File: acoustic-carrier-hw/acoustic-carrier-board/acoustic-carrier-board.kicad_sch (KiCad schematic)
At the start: 0 parts

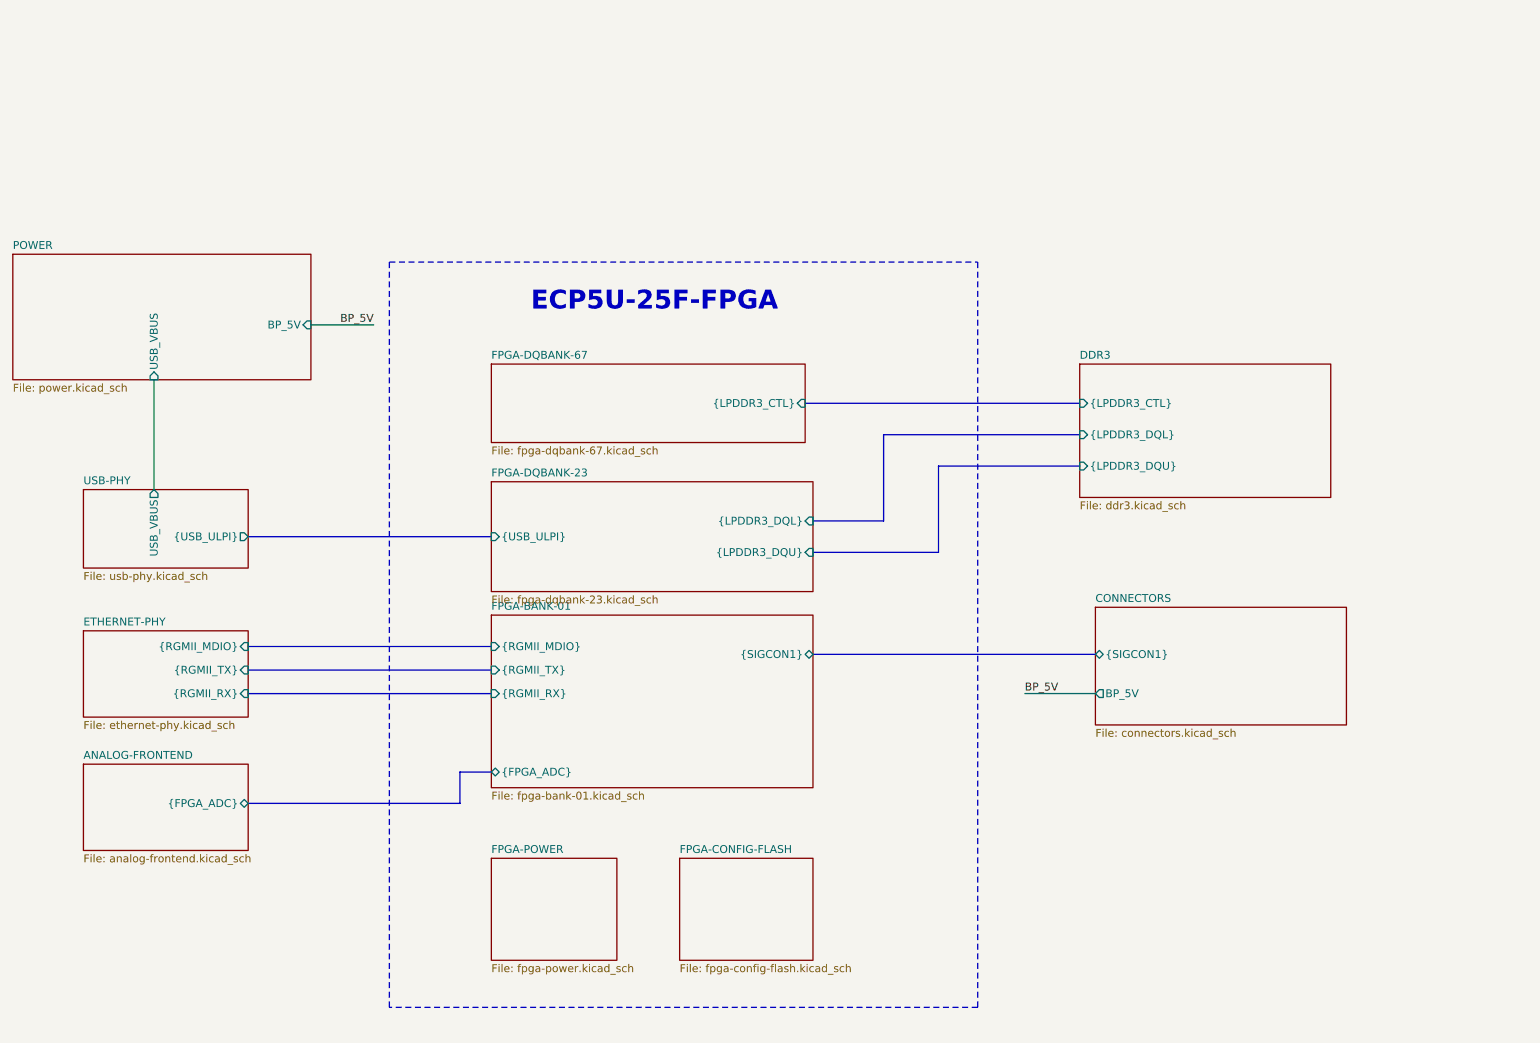
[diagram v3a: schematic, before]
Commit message: [carrier] Added decoupling caps to flash and comparators
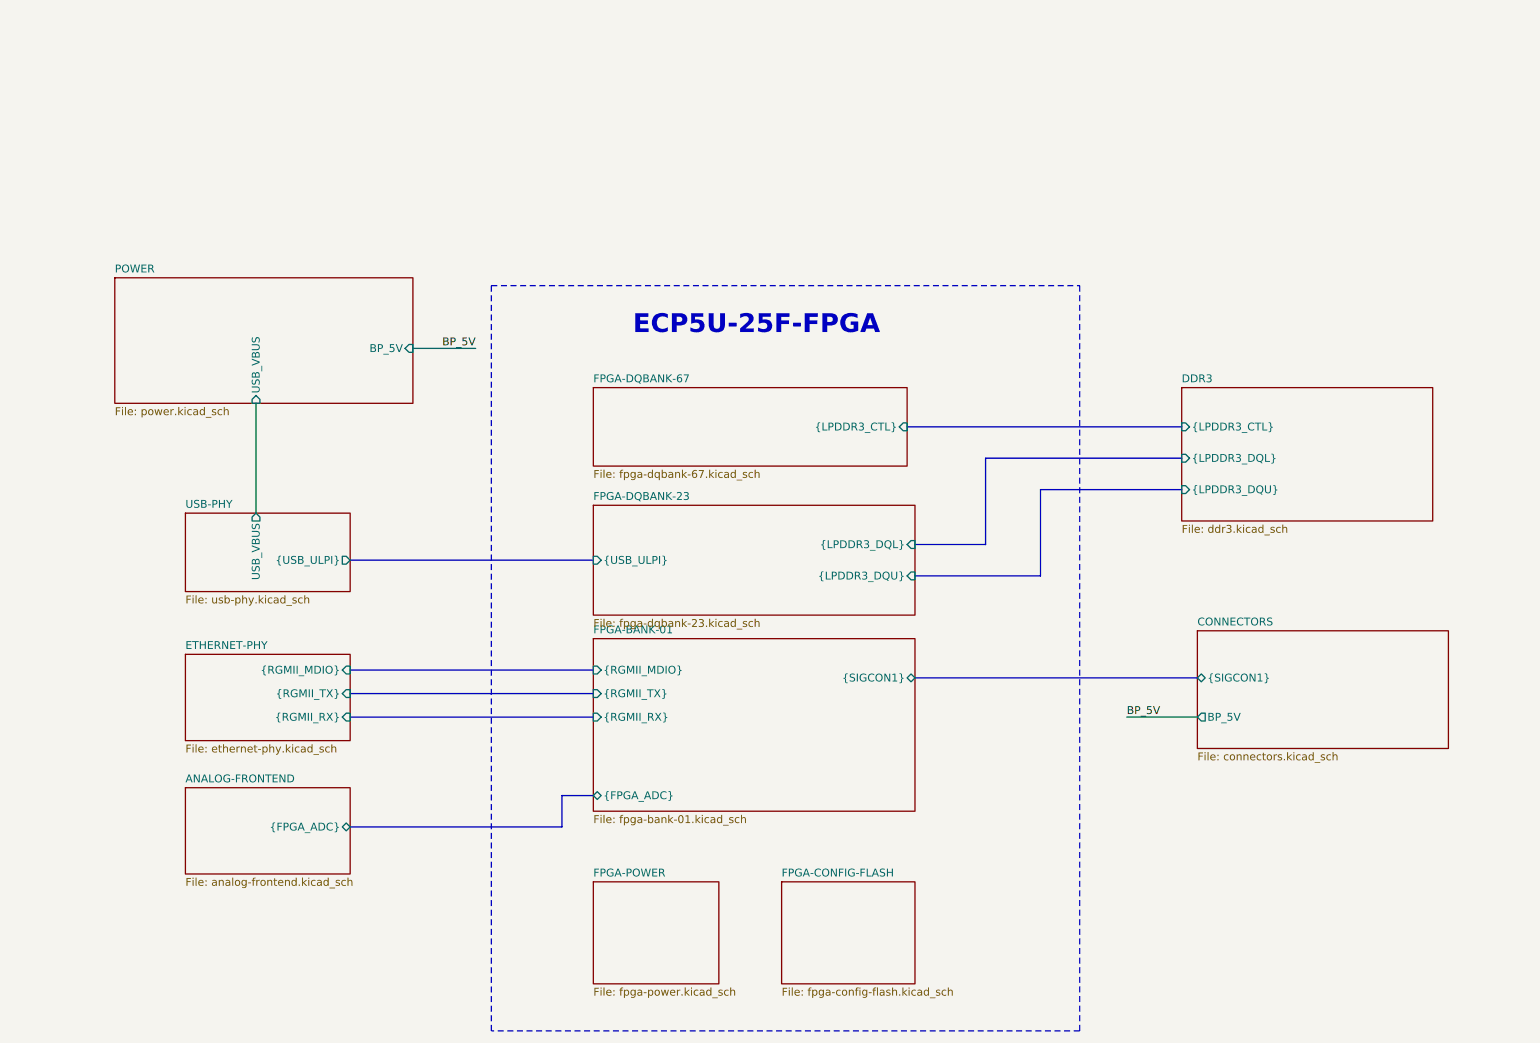
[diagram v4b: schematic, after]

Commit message: [carrier] Added extra decoupling to ECP5U according to datasheet (next) perform page-wise checks, add testpoints
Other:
- sheet CONNECTORS ports: added none; removed BP_5V
- sheet POWER ports: added none; removed BP_5V
- note added: "CONNECTORS - Connectors bound to a peripheral are kept in the same schematic - Connectors indifferent to FPGA bank are put in "connectors""
- note added: "DESIGN RULES"
- note added: "GENERAL FPGA NOTES"
- note added: "POWER RECOMMENDATIONS - Check 3.1 TN-02038 for filtering and decoupling - Used banks: extra decoupling capacitance"
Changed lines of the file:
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@@
+		)
+	)
+	(text "GENERAL FPGA NOTES"
+		(exclude_from_sim no)
+		(at 103.886 -9.652 0)
+		(effects
+			(font
+				(size 2.54 2.54)
+			)
+			(justify left bottom)
 		)
 	)
@@
 		)
 	)
-	(bus
-		(pts
-			(xy 180.34 57.15) (xy 212.09 57.15)
-		)
-		(stroke
-			(width 0)
-			(type default)
-		)
-	)
-	(bus
-		(pts
-			(xy 116.84 111.76) (xy 111.76 111.76)
-		)
-		(stroke
-			(width 0)
-			(type default)
-		)
-	)
-	(bus
-		(pts
-			(xy 189.23 62.23) (xy 212.09 62.23)
-		)
-		(stroke
-			(width 0)
-			(type default)
-		)
-	)
-	(bus
-		(pts
-			(xy 111.76 116.84) (xy 77.47 116.84)
-		)
-		(stroke
-			(width 0)
-			(type default)
-		)
-	)
-	(wire
-		(pts
-			(xy 62.23 48.26) (xy 62.23 66.04)
-		)
-		(stroke
-			(width 0)
-			(type default)
-		)
-	)
-	(wire
-		(pts
-			(xy 87.63 39.37) (xy 97.79 39.37)
-		)
-		(stroke
-			(width 0)
-			(type default)
-		)
-	)
-	(bus
-		(pts
-			(xy 77.47 73.66) (xy 116.84 73.66)
-		)
-		(stroke
-			(width 0)
-			(type default)
-		)
-	)
-	(bus
-		(pts
-			(xy 167.64 52.07) (xy 212.09 52.07)
-		)
-		(stroke
-			(width 0)
-			(type default)
-		)
-	)
-	(bus
-		(pts
-			(xy 189.23 76.2) (xy 168.91 76.2)
-		)
-		(stroke
-			(width 0)
-			(type default)
-		)
-	)
-	(bus
-		(pts
-			(xy 180.34 57.15) (xy 180.34 71.12)
-		)
-		(stroke
-			(width 0)
-			(type default)
-		)
-	)
-	(bus
-		(pts
-			(xy 111.76 111.76) (xy 111.76 116.84)
-		)
-		(stroke
-			(width 0)
-			(type default)
-		)
-	)
-	(bus
-		(pts
-			(xy 77.47 91.44) (xy 116.84 91.44)
-		)
-		(stroke
-			(width 0)
-			(type default)
-		)
-	)
-	(bus
-		(pts
-			(xy 168.91 92.71) (xy 214.63 92.71)
-		)
-		(stroke
-			(width 0)
-			(type default)
-		)
-	)
-	(bus
-		(pts
-			(xy 189.23 62.23) (xy 189.23 76.2)
-		)
-		(stroke
-			(width 0)
-			(type default)
-		)
-	)
-	(bus
-		(pts
-			(xy 77.47 99.06) (xy 116.84 99.06)
-		)
-		(stroke
-			(width 0)
-			(type default)
-		)
-	)
-	(wire
-		(pts
-			(xy 203.2 99.06) (xy 214.63 99.06)
-		)
-		(stroke
-			(width 0)
-			(type default)
-		)
-	)
-	(bus
-		(pts
-			(xy 77.47 95.25) (xy 116.84 95.25)
-		)
-		(stroke
-			(width 0)
-			(type default)
-		)
-	)
-	(bus
-		(pts
-			(xy 180.34 71.12) (xy 168.91 71.12)
-		)
-		(stroke
-			(width 0)
-			(type default)
-		)
-	)
-	(label "BP_5V"
-		(at 203.2 99.06 0)
+	(text "POWER RECOMMENDATIONS\n- Check 3.1 TN-02038 for filtering and decoupling\n- Used banks: extra decoupling capacitance"
+		(exclude_from_sim no)
+		(at 104.394 -1.778 0)
 		(effects
 			(font
@@
 		)
 	)
-	(label "BP_5V"
-		(at 97.79 39.37 180)
+	(text "CONNECTORS\n- Connectors bound to a peripheral are kept in the same schematic\n- Connectors indifferent to FPGA bank are put in \"connectors\""
+		(exclude_from_sim no)
+		(at 188.468 -2.794 0)
 		(effects
 			(font
 				(size 1.27 1.27)
 			)
-			(justify right bottom)
+			(justify left bottom)
+		)
+	)
+	(text "DESIGN RULES"
+		(exclude_from_sim no)
+		(at 187.96 -10.668 0)
+		(effects
+			(font
+				(size 2.54 2.54)
+			)
+			(justify left bottom)
+		)
+	)
+	(bus
+		(pts
+			(xy 180.34 57.15) (xy 212.09 57.15)
+		)
+		(stroke
+			(width 0)
+			(type default)
+		)
+	)
+	(bus
+		(pts
+			(xy 116.84 111.76) (xy 111.76 111.76)
+		)
+		(stroke
+			(width 0)
+			(type default)
+		)
+	)
+	(bus
+		(pts
+			(xy 189.23 62.23) (xy 212.09 62.23)
+		)
+		(stroke
+			(width 0)
+			(type default)
+		)
+	)
+	(bus
+		(pts
+			(xy 111.76 116.84) (xy 77.47 116.84)
+		)
+		(stroke
+			(width 0)
+			(type default)
+		)
+	)
+	(wire
+		(pts
+			(xy 62.23 48.26) (xy 62.23 66.04)
+		)
+		(stroke
+			(width 0)
+			(type default)
+		)
+	)
+	(bus
+		(pts
+			(xy 77.47 73.66) (xy 116.84 73.66)
+		)
+		(stroke
+			(width 0)
+			(type default)
+		)
+	)
+	(bus
+		(pts
+			(xy 167.64 52.07) (xy 212.09 52.07)
+		)
+		(stroke
+			(width 0)
+			(type default)
+		)
+	)
+	(bus
+		(pts
+			(xy 189.23 76.2) (xy 168.91 76.2)
+		)
+		(stroke
+			(width 0)
+			(type default)
+		)
+	)
+	(bus
+		(pts
+			(xy 180.34 57.15) (xy 180.34 71.12)
+		)
+		(stroke
+			(width 0)
+			(type default)
+		)
+	)
+	(bus
+		(pts
+			(xy 111.76 111.76) (xy 111.76 116.84)
+		)
+		(stroke
+			(width 0)
+			(type default)
+		)
+	)
+	(bus
+		(pts
+			(xy 77.47 91.44) (xy 116.84 91.44)
+		)
+		(stroke
+			(width 0)
+			(type default)
+		)
+	)
+	(bus
+		(pts
+			(xy 168.91 92.71) (xy 213.36 92.71)
+		)
+		(stroke
+			(width 0)
+			(type default)
+		)
+	)
+	(bus
+		(pts
+			(xy 189.23 62.23) (xy 189.23 76.2)
+		)
+		(stroke
+			(width 0)
+			(type default)
+		)
+	)
+	(bus
+		(pts
+			(xy 77.47 99.06) (xy 116.84 99.06)
+		)
+		(stroke
+			(width 0)
+			(type default)
+		)
+	)
+	(bus
+		(pts
+			(xy 77.47 95.25) (xy 116.84 95.25)
+		)
+		(stroke
+			(width 0)
+			(type default)
+		)
+	)
+	(bus
+		(pts
+			(xy 180.34 71.12) (xy 168.91 71.12)
+		)
+		(stroke
+			(width 0)
+			(type default)
 		)
 	)
@@
 				)
 				(justify left)
-			)
-		)
-		(pin "BP_5V" input
-			(at 87.63 39.37 0)
-			(effects
-				(font
-					(size 1.27 1.27)
-				)
-				(justify right)
 			)
 		)
@@
 	)
 	(sheet
-		(at 147.32 125.73)
-		(size 21.59 16.51)
+		(at 149.86 125.73)
+		(size 43.18 16.51)
 		(exclude_from_sim no)
 		(in_bom yes)
@@
 		)
 		(property "Sheetname" "FPGA-CONFIG-FLASH"
-			(at 147.32 125.0184 0)
+			(at 149.86 125.0184 0)
 			(effects
 				(font
@@
 		)
 		(property "Sheetfile" "fpga-config-flash.kicad_sch"
-			(at 147.32 142.8246 0)
+			(at 149.86 142.8246 0)
 			(effects
 				(font
@@
 	)
 	(sheet
-		(at 116.84 125.73)
-		(size 20.32 16.51)
+		(at 104.14 125.73)
+		(size 39.37 16.51)
 		(exclude_from_sim no)
 		(in_bom yes)
@@
 		)
 		(property "Sheetname" "FPGA-POWER"
-			(at 116.84 125.0184 0)
+			(at 104.14 125.0184 0)
 			(effects
 				(font
@@
 		)
 		(property "Sheetfile" "fpga-power.kicad_sch"
-			(at 116.84 142.8246 0)
+			(at 104.14 142.8246 0)
 			(effects
 				(font
@@
 		)
 		(property "Field2" ""
-			(at 116.84 125.73 0)
+			(at 104.14 125.73 0)
 			(effects
 				(font
@@
 	)
 	(sheet
-		(at 214.63 85.09)
+		(at 213.36 85.09)
 		(size 40.64 19.05)
 		(exclude_from_sim no)
@@
 		)
 		(property "Sheetname" "CONNECTORS"
-			(at 214.63 84.3784 0)
+			(at 213.36 84.3784 0)
 			(effects
 				(font
@@
 		)
 		(property "Sheetfile" "connectors.kicad_sch"
-			(at 214.63 104.7246 0)
+			(at 213.36 104.7246 0)
 			(effects
 				(font
@@
 		)
 		(pin "{SIGCON1}" bidirectional
-			(at 214.63 92.71 180)
-			(effects
-				(font
-					(size 1.27 1.27)
-				)
-				(justify left)
-			)
-		)
-		(pin "BP_5V" output
-			(at 214.63 99.06 180)
-			(effects
-				(font
+			(at 213.36 92.71 180)
+			(effects
+				(font
